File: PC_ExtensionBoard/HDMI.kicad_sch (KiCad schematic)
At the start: 38 parts, among them Q10 2SK3018, Q11 2N7002, Q6 2SK3018, Q9 2SK3018, U5 TPAZ1023-04F, U6 TPAZ1023-04F

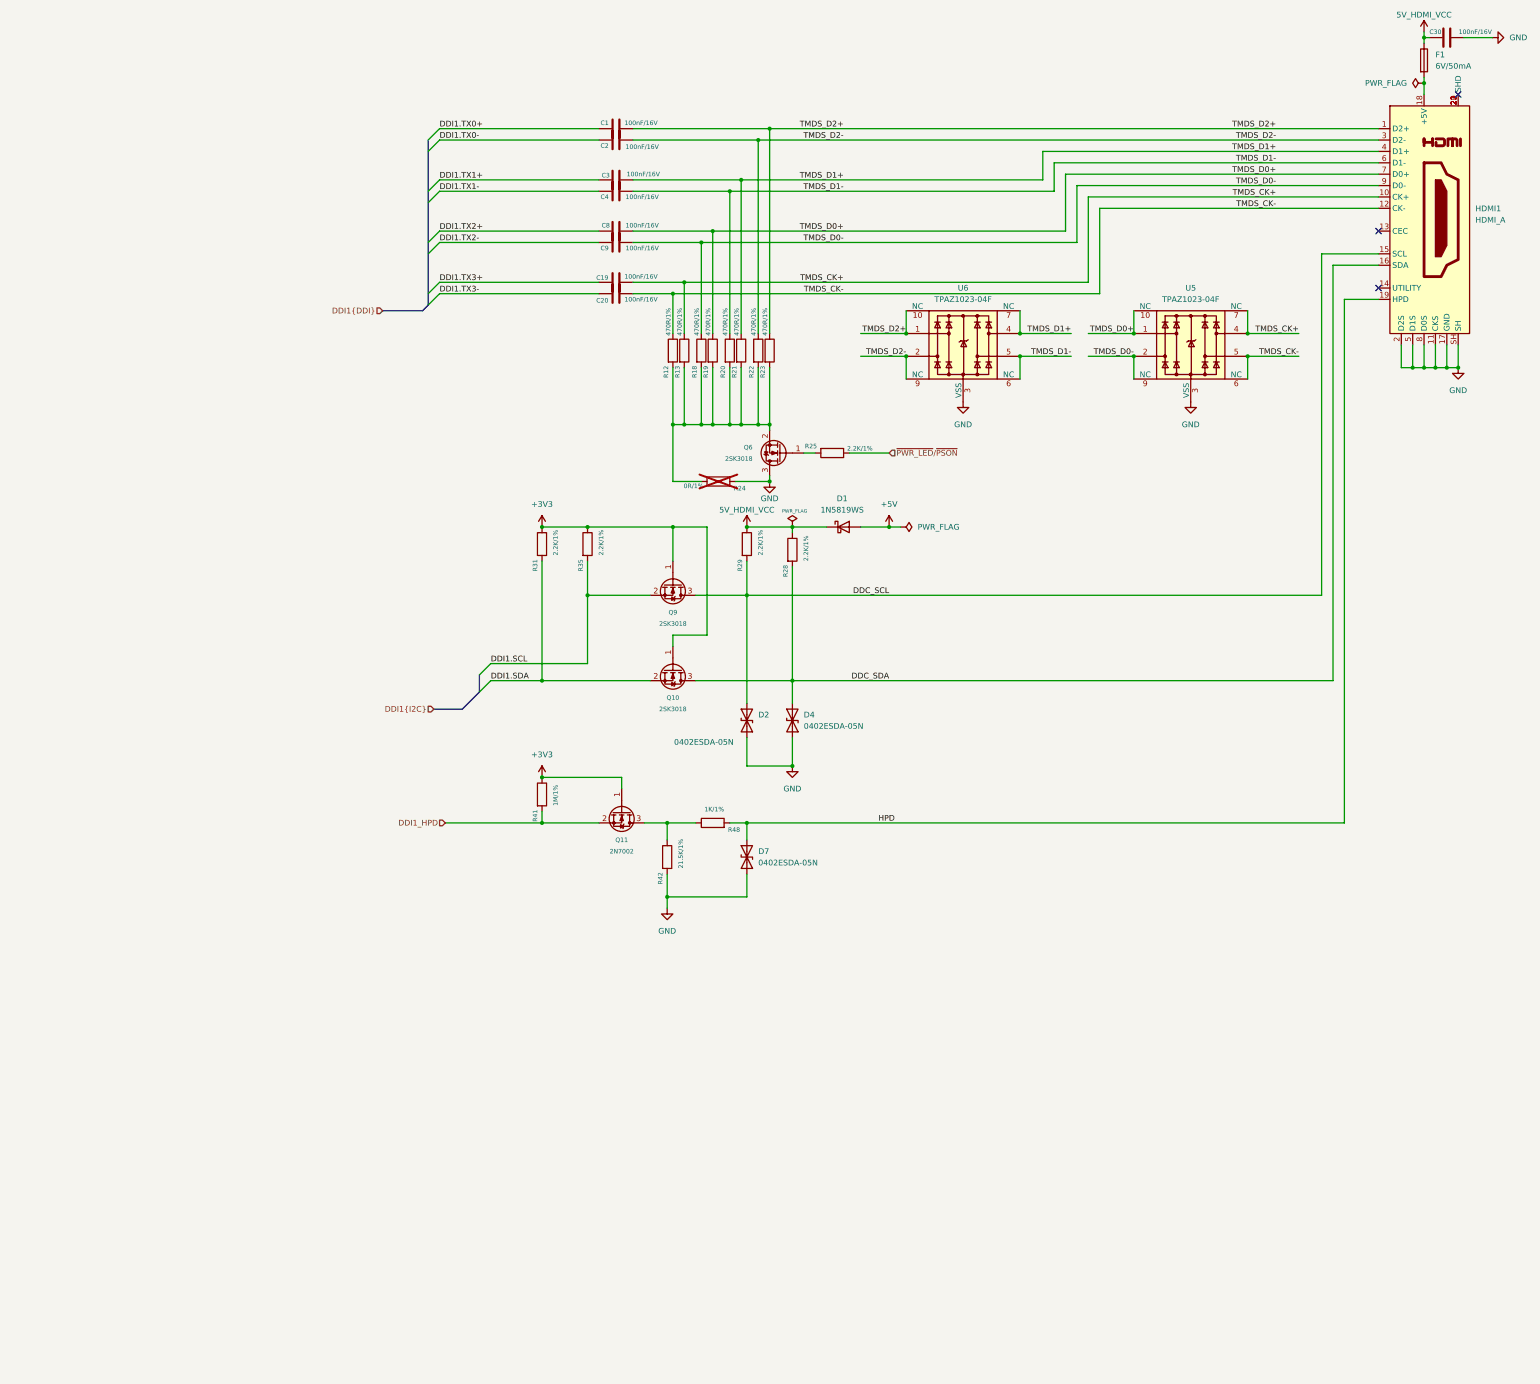
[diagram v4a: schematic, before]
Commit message: update LCSC for HDMI
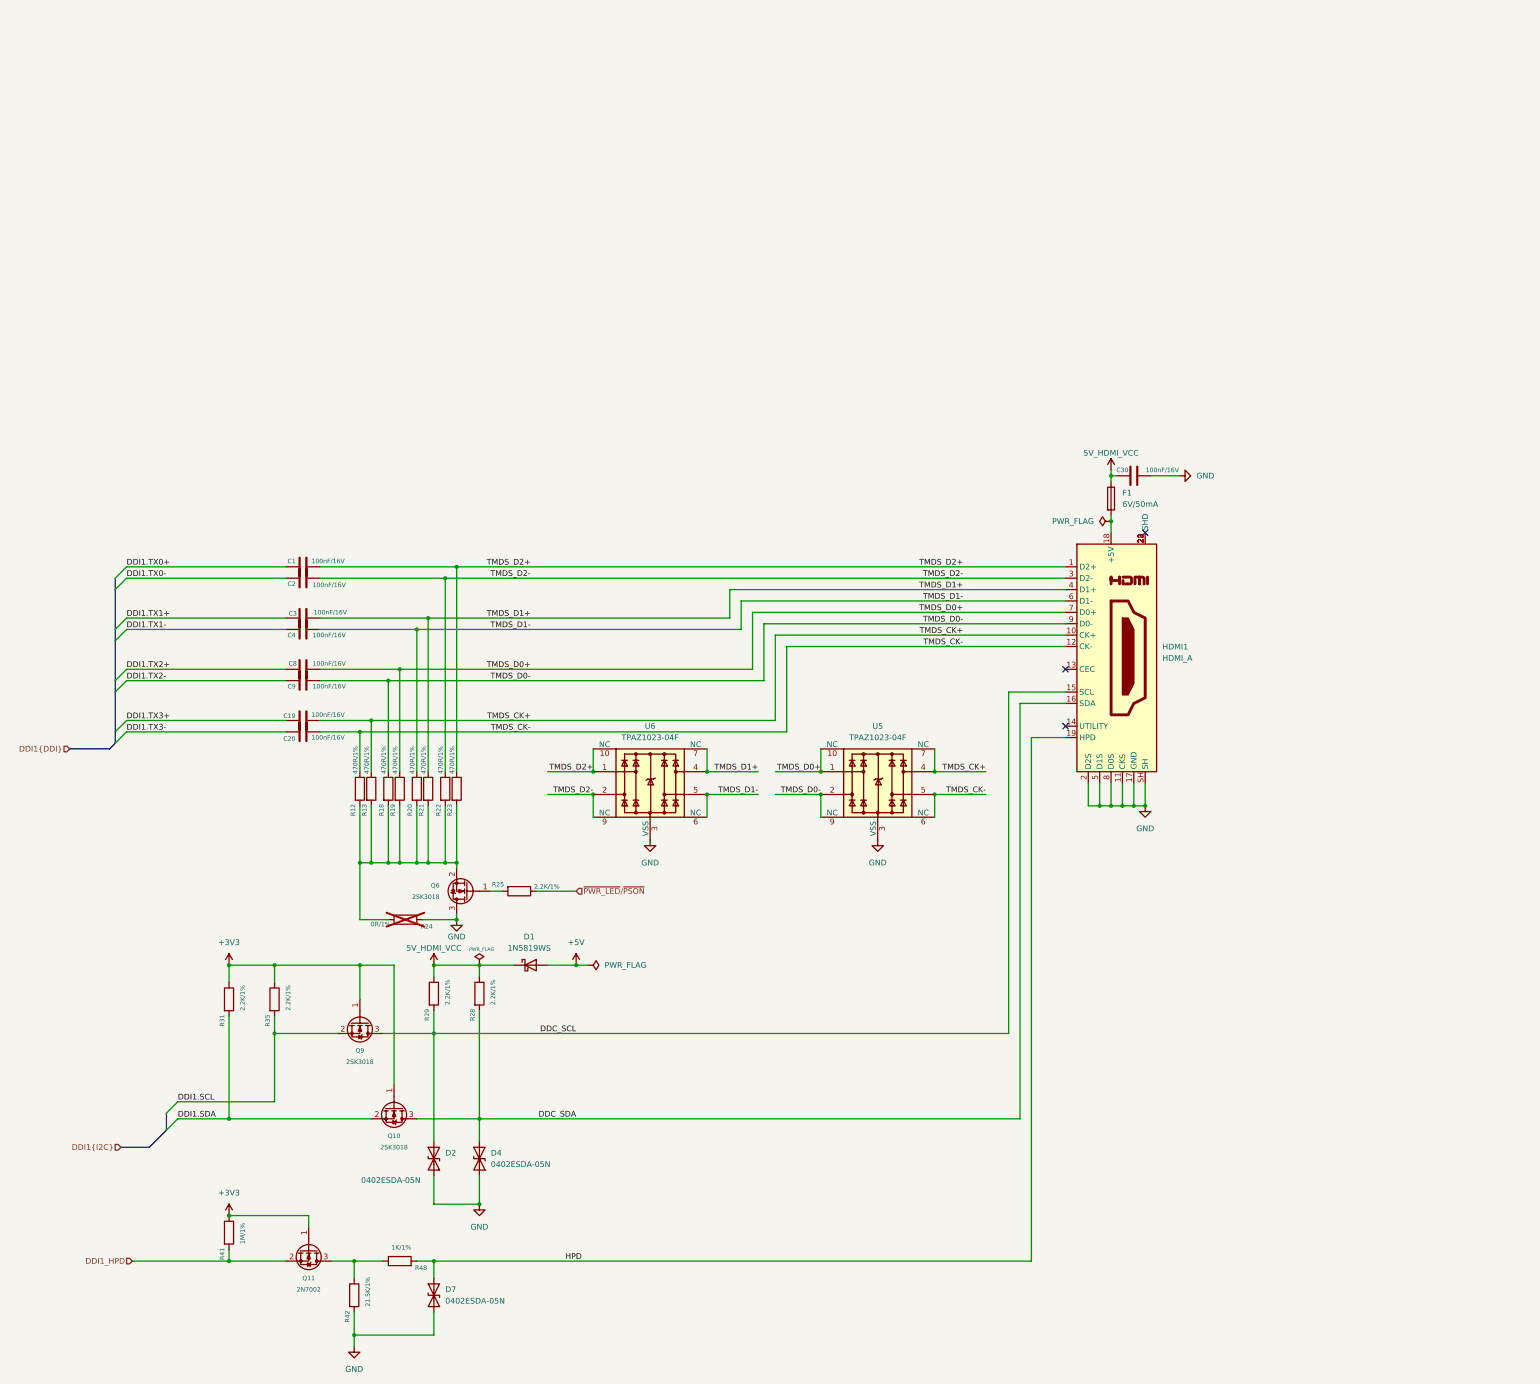
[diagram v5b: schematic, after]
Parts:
- C1, C19, C2, C20, C3, C4, C8, C9: LCSC (none) -> C85960
- C30: footprint A_HDJ_Library:C_0402_1005Metric -> Capacitor_SMD:C_0402_1005Metric; DF_Comment 贴片电容0402-100nF-16V-X7R(0402) -> (none); LCSC (none) -> C85960
- D1: footprint PC_Components_1:SOT-323 -> PC_Components_1:D_SOD-323; LCSC (none) -> C191023
- D2, D4: LCSC (none) -> C316049
- D7: footprint A_HDJ_Library:D_0402_1005Metric -> Diode_SMD:D_0402_1005Metric; LCSC (none) -> C316049
- F1: Buy_Link https://item.szlcsc.com/8530937.html -> (none); DF_Comment 0603贴片自恢复保险丝0.05A-6V_0603L005-6AR -> (none); LCSC (none) -> C7472508; SCH_Show_Footprint R0805 -> (none)
- HDMI1: footprint A_HDJ_Library:HDMI_A_Molex_208658-1001_Horizontal -> PC_Components_1:HDMI-SMD_HDMI-019S
- Q10, Q6, Q9: LCSC (none) -> C727148
- Q11: LCSC (none) -> C8545
- R24, R25, R28, R29, R31, R35: footprint (none) -> PC_Components_1:R_0402_1005Metric; LCSC (none) -> C25879
- R41: footprint (none) -> PC_Components_1:R_0402_1005Metric; LCSC (none) -> C26083
- R42: footprint (none) -> PC_Components_1:R_0402_1005Metric; LCSC (none) -> C25872
- R48: footprint (none) -> PC_Components_1:R_0402_1005Metric; LCSC (none) -> C11702
- U5, U6: LCSC (none) -> C2827676
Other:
- moved on the sheet: C1, C19, C2, C20, C3, C30, C4, C8, C9, D1, D2, D4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

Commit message: update LCSC
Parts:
- added J1: Conn_01x26_MountingPin, PC_Components_1:FPC-SMD_24P-P0.50_FPC-05F-24PH20, symbol Connector_Generic_MountingPin:Conn_01x26_MountingPin
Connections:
- net 5V_HDMI_VCC: now also J1.23 (Pin_23), J1.24 (Pin_24)
- net GND: now also J1.1 (Pin_1), J1.10 (Pin_10), J1.13 (Pin_13), J1.14 (Pin_14), J1.16 (Pin_16), J1.18 (Pin_18), J1.20 (Pin_20), J1.22 (Pin_22), J1.25 (Pin_25), J1.26 (Pin_26), J1.4 (Pin_4), J1.7 (Pin_7)
- new net DDI2.SCL: J1.17 (Pin_17)
- new net DDI2.SDA: J1.19 (Pin_19)
- new net DDI2.TX0+: J1.8 (Pin_8)
- new net DDI2.TX0-: J1.9 (Pin_9)
- new net DDI2.TX1+: J1.5 (Pin_5)
- new net DDI2.TX1-: J1.6 (Pin_6)
- new net DDI2.TX2+: J1.2 (Pin_2)
- new net DDI2.TX2-: J1.3 (Pin_3)
- new net DDI2.TX3+: J1.11 (Pin_11)
- new net DDI2.TX3-: J1.12 (Pin_12)
- new net DDI2_HPD: J1.21 (Pin_21)
- no-connect marks 3 -> 4
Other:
- note added: "HDMI-1"
- note added: "HDMI2-Socket"
- moved on the sheet: C1, C19, C2, C20, C3, C30, C4, C8, C9, D1, D2, D4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

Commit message: schematic changes
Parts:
- added C115, C116: C_100n_0402, PC_Components_1:C_0402_1005Metric, symbol A_PC_ExtensionBoard:C_100n_0402
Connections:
- net +5V: now also C115.2, C116.2
- net GND: now also C115.1, C116.1

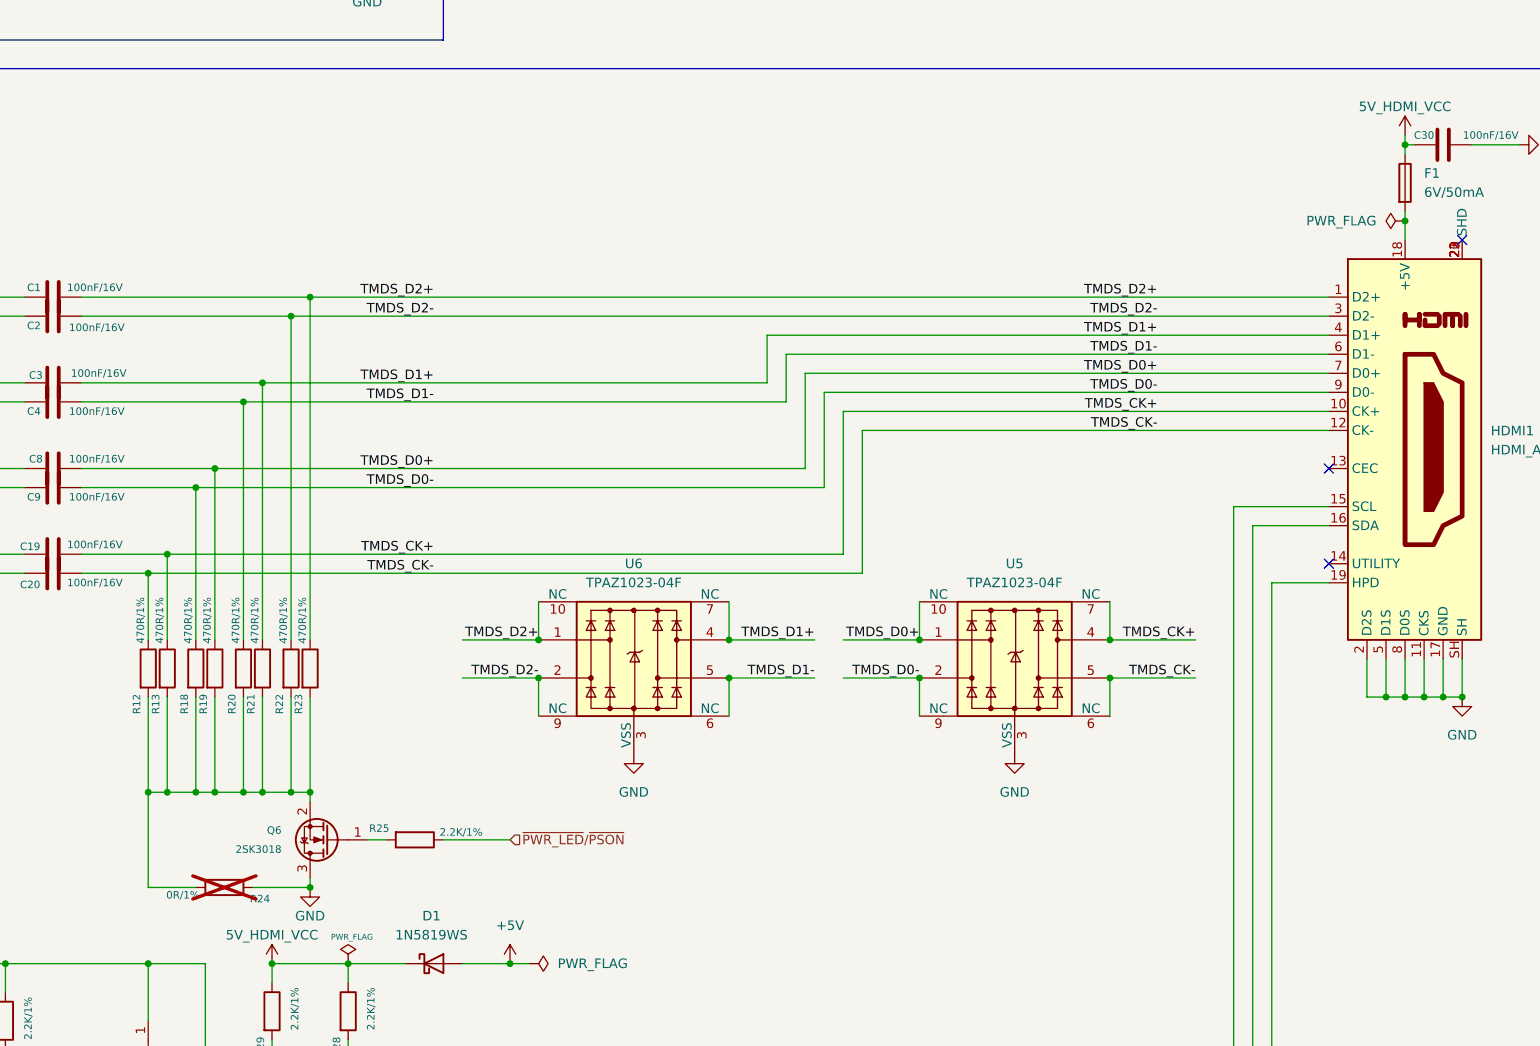
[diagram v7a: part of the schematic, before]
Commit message: update schematic
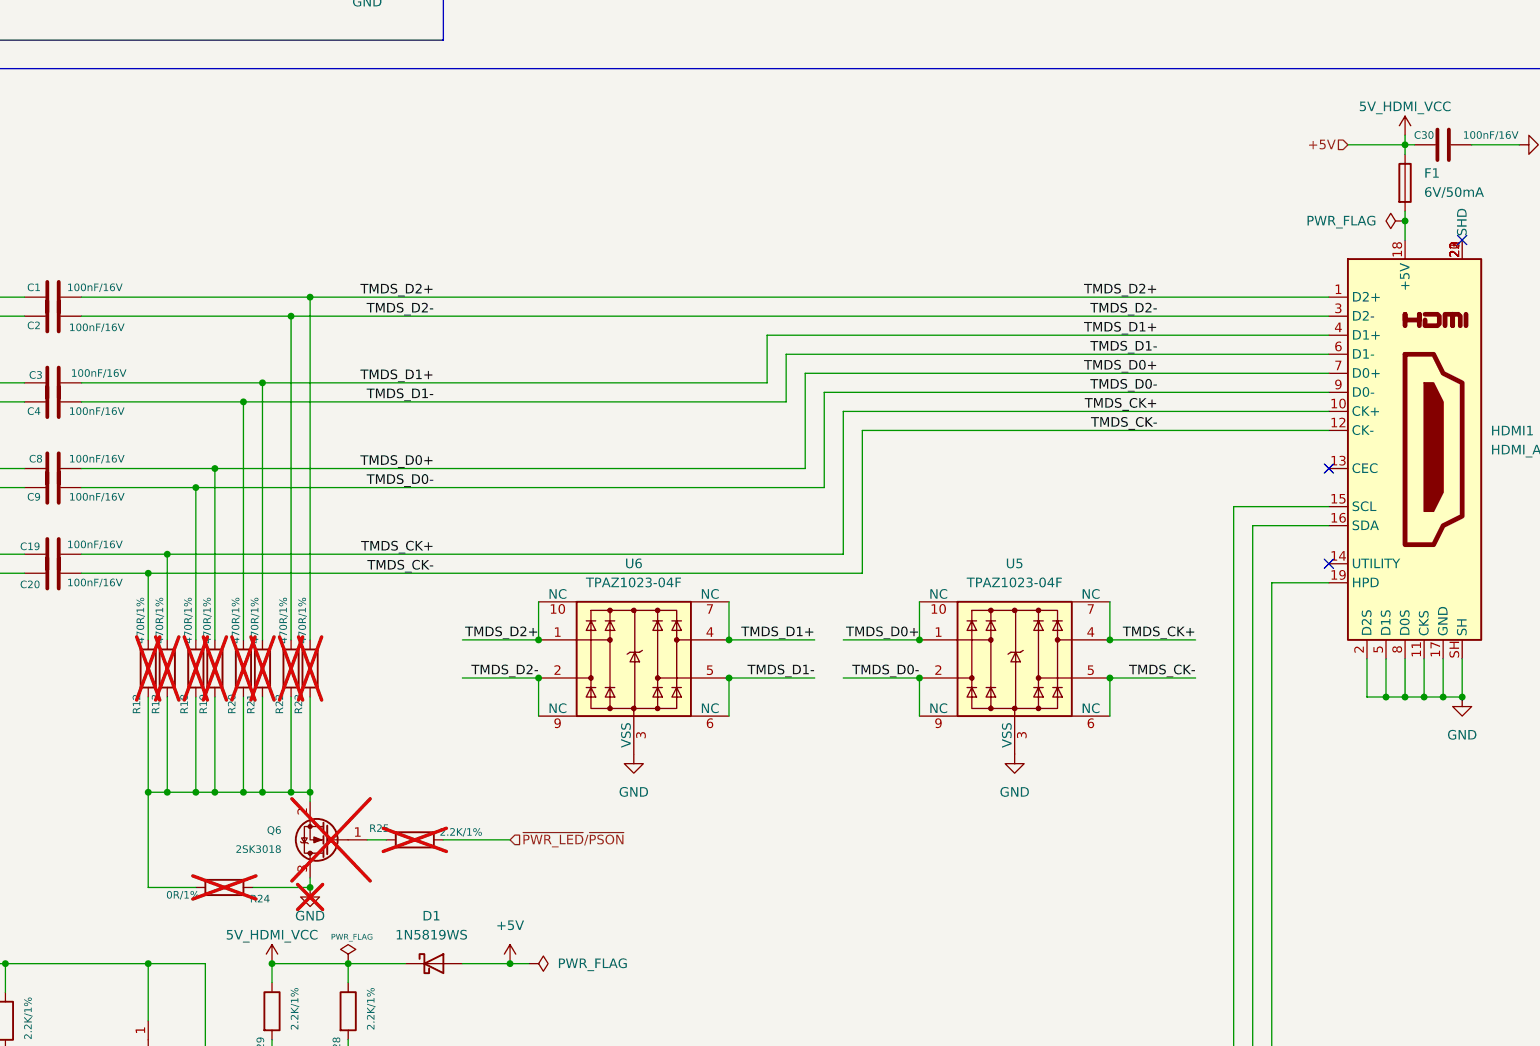
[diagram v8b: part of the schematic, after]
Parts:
- Q6, R25: now not fitted
- R12, R13, R18, R19, R20, R21, R22, R23: now not fitted; now left out of the parts list
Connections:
- net 5V_HDMI_VCC is gone; now on net +5V: C30.1, D1.1 (K), F1.1, J1.23 (Pin_23), J1.24 (Pin_24), R28.1, R29.1
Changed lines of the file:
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@@
 		)
 	)
+	(wire
+		(pts
+			(xy 270.51 203.2) (xy 278.13 203.2)
+		)
+		(stroke
+			(width 0)
+			(type default)
+		)
+	)
 	(bus
 		(pts
@@
 		)
 	)
+	(hierarchical_label "+5V"
+		(shape input)
+		(at 270.51 203.2 180)
+		(effects
+			(font
+				(size 1.27 1.27)
+			)
+			(justify right)
+		)
+	)
 	(hierarchical_label "DDI1{DDI}"
 		(shape input)
@@
 		(body_style 1)
 		(exclude_from_sim no)
-		(in_bom yes)
-		(on_board yes)
+		(in_bom no)
+		(on_board no)
 		(in_pos_files yes)
-		(dnp no)
+		(dnp yes)
 		(property "Reference" "R22"
 			(at 128.016 279.146 90)
@@
 		(body_style 1)
 		(exclude_from_sim no)
-		(in_bom yes)
-		(on_board yes)
+		(in_bom no)
+		(on_board no)
 		(in_pos_files yes)
-		(dnp no)
+		(dnp yes)
 		(property "Reference" "R23"
 			(at 130.556 279.146 90)
@@
 		(body_style 1)
 		(exclude_from_sim no)
-		(in_bom yes)
-		(on_board yes)
+		(in_bom no)
+		(on_board no)
 		(in_pos_files yes)
-		(dnp no)
+		(dnp yes)
 		(property "Reference" "R21"
 			(at 124.206 279.146 90)
@@
 		(body_style 1)
 		(exclude_from_sim no)
-		(in_bom yes)
-		(on_board yes)
+		(in_bom no)
+		(on_board no)
 		(in_pos_files yes)
-		(dnp no)
+		(dnp yes)
 		(property "Reference" "R13"
 			(at 111.506 279.146 90)
@@
 		(exclude_from_sim no)
 		(in_bom yes)
-		(on_board yes)
+		(on_board no)
 		(in_pos_files yes)
-		(dnp no)
+		(dnp yes)
 		(property "Reference" "#PWR039"
 			(at 132.08 308.61 0)
@@
 		(body_style 1)
 		(exclude_from_sim no)
-		(in_bom yes)
-		(on_board yes)
+		(in_bom no)
+		(on_board no)
 		(in_pos_files yes)
-		(dnp no)
+		(dnp yes)
 		(property "Reference" "R19"
 			(at 117.856 279.146 90)
@@
 		(body_style 1)
 		(exclude_from_sim no)
-		(in_bom yes)
-		(on_board yes)
+		(in_bom no)
+		(on_board no)
 		(in_pos_files yes)
-		(dnp no)
+		(dnp yes)
 		(property "Reference" "R18"
 			(at 115.316 279.146 90)
@@
 		(exclude_from_sim no)
 		(in_bom yes)
-		(on_board yes)
+		(on_board no)
 		(in_pos_files yes)
-		(dnp no)
+		(dnp yes)
 		(property "Reference" "R25"
 			(at 139.954 294.386 90)
@@
 		(exclude_from_sim no)
 		(in_bom yes)
-		(on_board yes)
+		(on_board no)
 		(in_pos_files yes)
-		(dnp no)
+		(dnp yes)
 		(fields_autoplaced yes)
 		(property "Reference" "Q6"
@@
 		(body_style 1)
 		(exclude_from_sim no)
-		(in_bom yes)
-		(on_board yes)
+		(in_bom no)
+		(on_board no)
 		(in_pos_files yes)
-		(dnp no)
+		(dnp yes)
 		(property "Reference" "R12"
 			(at 108.966 279.146 90)
@@
 		(exclude_from_sim no)
 		(in_bom no)
-		(on_board yes)
+		(on_board no)
 		(in_pos_files yes)
 		(dnp yes)
@@
 		(body_style 1)
 		(exclude_from_sim no)
-		(in_bom yes)
-		(on_board yes)
+		(in_bom no)
+		(on_board no)
 		(in_pos_files yes)
-		(dnp no)
+		(dnp yes)
 		(property "Reference" "R20"
 			(at 121.666 279.146 90)
